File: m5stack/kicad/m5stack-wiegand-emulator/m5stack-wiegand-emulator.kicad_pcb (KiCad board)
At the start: 2 copper layers, 50 x 50 mm, 58 parts, among them J1 2x15 socket header, J2 2x15 pin header, J3 1x5 female, M1 M5 Stack 3.1mm mounting hole, M12 M5 Stack 1.1mm reference hole, M2 M5 Stack 3.1mm mounting hole, M3 M5 Stack 3.1mm mounting hole, M4 M5 Stack 3.1mm mounting hole, M5 M5 Stack 2mm mounting hole, M6 M5 Stack 2mm mounting hole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

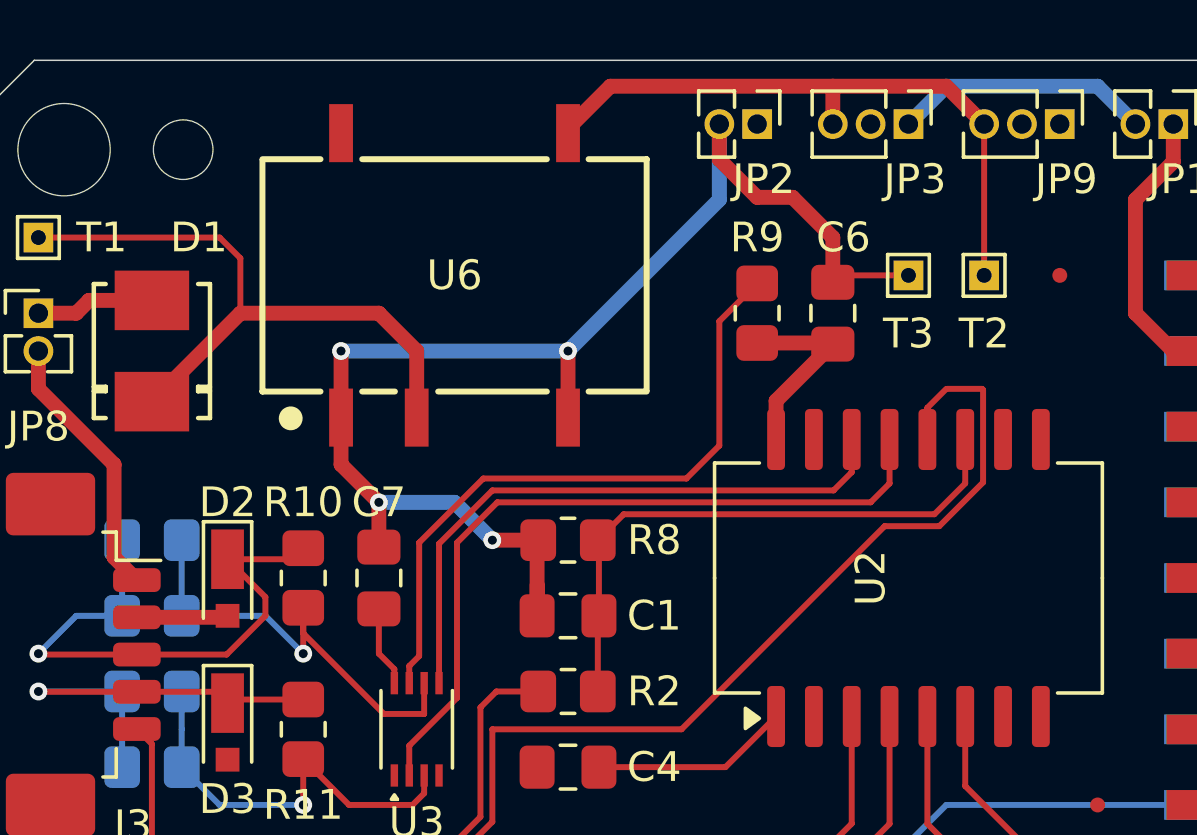
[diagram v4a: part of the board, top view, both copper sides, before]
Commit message: M5: recalculated LED input resistance
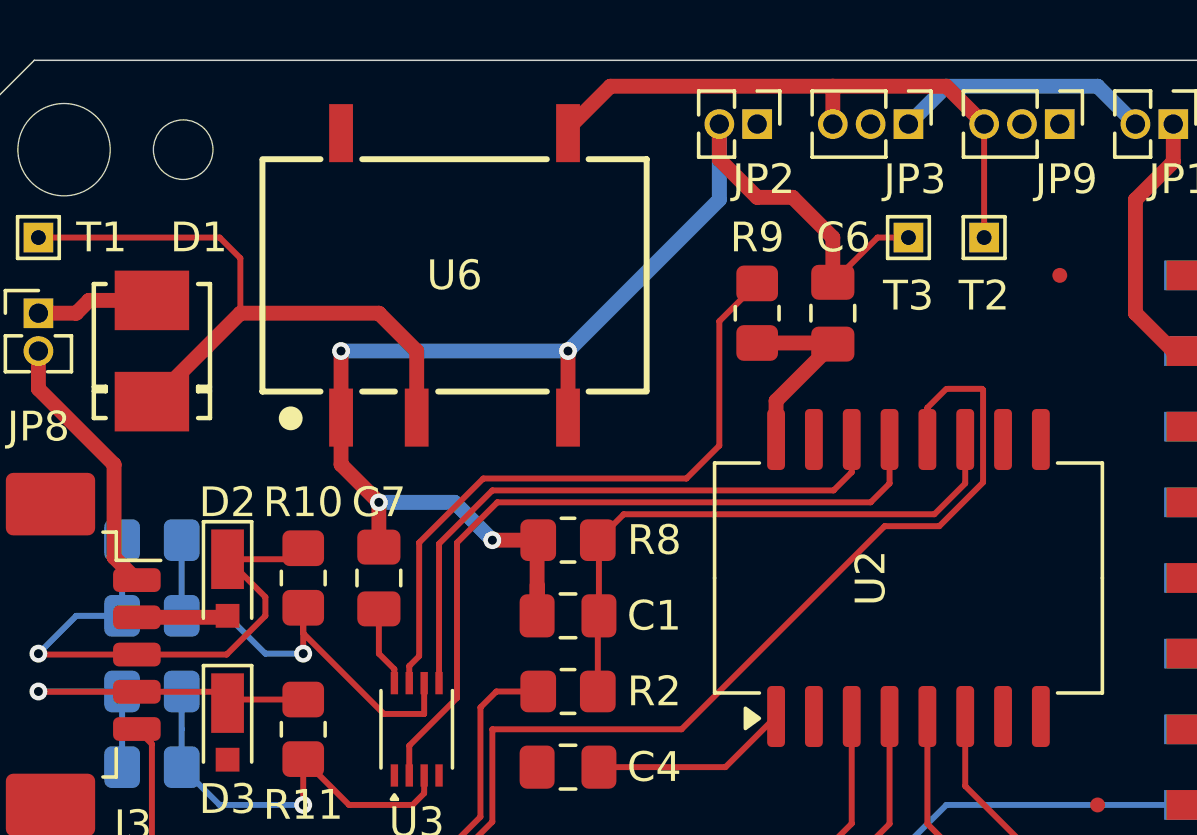
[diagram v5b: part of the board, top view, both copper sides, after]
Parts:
- R13: value 10 -> 1k
- R2: value 470 -> 1k
- moved T2 1.27 mm to (123.2, 69.8)
- moved T3 1.27 mm to (120.7, 69.8)
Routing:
- net +VDC: track 21.6 -> 20.3 mm
- net GND1: track 53.4 -> 53.9 mm
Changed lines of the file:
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@@
     (pad "2" smd rect (at 1.02 0 270) (size 0.8 0.8) (layers "F.Cu" "F.Paste" "F.Mask")
       (net 62 "GND1") (pinfunction "A2") (pintype "passive"))
-    (model "${KICAD6_3DMODEL_DIR}/Diode_SMD.3dshapes/D_MicroSMP_AK.wrl"
+    (model "${KICAD_UHPPOTED}/uhppoted.pretty/MSP5.0A-M3_89A.step" hide
       (offset (xyz 0 0 0))
       (scale (xyz 1 1 1))
-      (rotate (xyz 0 0 0))
+      (rotate (xyz -90 0 0))
+    )
+    (model "${KICAD_UHPPOTED}/uhppoted.pretty/DO-219AD.step"
+      (offset (xyz 0 0 0))
+      (scale (xyz 1 1 1))
+      (rotate (xyz -90 0 0))
     )
   )
@@
     (pad "2" smd rect (at 1.02 0 270) (size 0.8 0.8) (layers "F.Cu" "F.Paste" "F.Mask")
       (net 62 "GND1") (pinfunction "A2") (pintype "passive"))
-    (model "${KICAD6_3DMODEL_DIR}/Diode_SMD.3dshapes/D_MicroSMP_AK.wrl"
+    (model "${KICAD_UHPPOTED}/uhppoted.pretty/MSP5.0A-M3_89A.step" hide
       (offset (xyz 0 0 0))
       (scale (xyz 1 1 1))
-      (rotate (xyz 0 0 0))
+      (rotate (xyz -90 0 0))
+    )
+    (model "${KICAD_UHPPOTED}/uhppoted.pretty/DO-219AD.step"
+      (offset (xyz 0 0 0))
+      (scale (xyz 1 1 1))
+      (rotate (xyz -90 0 0))
     )
   )
@@
     (property "ki_keywords" "diode TVS thyrector")
     (attr smd)
-    (fp_text reference "D2" (at -2.79 0 180) (layer "F.SilkS")
+    (fp_text reference "D2" (at -2.79 0) (layer "F.SilkS")
         (effects (font (size 1 1) (thickness 0.15)))
     )
@@
     (pad "2" smd rect (at 1.02 0 270) (size 0.8 0.8) (layers "F.Cu" "F.Paste" "F.Mask")
       (net 62 "GND1") (pinfunction "A2") (pintype "passive"))
-    (model "${KICAD6_3DMODEL_DIR}/Diode_SMD.3dshapes/D_MicroSMP_AK.wrl"
+    (model "${KICAD_UHPPOTED}/uhppoted.pretty/MSP5.0A-M3_89A.step" hide
       (offset (xyz 0 0 0))
       (scale (xyz 1 1 1))
-      (rotate (xyz 0 0 0))
+      (rotate (xyz -90 0 0))
+    )
+    (model "${KICAD_UHPPOTED}/uhppoted.pretty/DO-219AD.step"
+      (offset (xyz 0 0 0))
+      (scale (xyz 1 1 1))
+      (rotate (xyz -90 0 0))
     )
   )
@@
         (effects (font (size 1 1) (thickness 0.15)) (justify right))
     )
-    (fp_text value "470" (at 0 1.65) (layer "F.Fab") hide
+    (fp_text value "1k" (at 0 1.65) (layer "F.Fab") hide
         (effects (font (size 1 1) (thickness 0.15)))
     )
@@
         (effects (font (size 1 1) (thickness 0.15)))
     )
-    (fp_text value "10" (at 0 1.65 90) (layer "F.Fab") hide
+    (fp_text value "1k" (at 0 1.65 90) (layer "F.Fab") hide
         (effects (font (size 1 1) (thickness 0.15)))
     )
@@
   )
   (footprint "TestPoint:TestPoint_THTPad_1.0x1.0mm_Drill0.5mm" (layer "F.Cu")
-    (at 123.19 71.12 180)
+    (at 123.19 69.85 180)
     (descr "THT rectangular pad as test Point, square 1.0mm side length, hole diameter 0.5mm")
     (tags "test point THT pad rectangle square")
@@
   )
   (footprint "TestPoint:TestPoint_THTPad_1.0x1.0mm_Drill0.5mm" (layer "F.Cu")
-    (at 120.65 71.12 180)
+    (at 120.65 69.85 180)
     (descr "THT rectangular pad as test Point, square 1.0mm side length, hole diameter 0.5mm")
     (tags "test point THT pad rectangle square")
@@
   (segment (start 100.33 83.135256) (end 103.039058 85.844314) (width 0.2) (layer "F.Cu") (net 42))
   (via (at 100.33 83.82) (size 0.6) (drill 0.3) (layers "F.Cu" "B.Cu") (net 42))
+  (segment (start 100.33 83.82) (end 99.06 83.82) (width 0.2) (layer "B.Cu") (net 42))
+  (segment (start 97.79 82.55) (end 96.25 82.55) (width 0.2) (layer "B.Cu") (net 42))
+  (segment (start 99.06 83.82) (end 97.79 82.55) (width 0.2) (layer "B.Cu") (net 42))
   (segment (start 96.25 80.01) (end 96.25 82.55) (width 0.2) (layer "B.Cu") (net 42))
-  (segment (start 99.06 82.55) (end 96.25 82.55) (width 0.2) (layer "B.Cu") (net 42))
-  (segment (start 100.33 83.82) (end 99.06 82.55) (width 0.2) (layer "B.Cu") (net 42))
-  (segment (start 123.19 71.12) (end 123.19 66.04) (width 0.2) (layer "F.Cu") (net 44))
   (segment (start 121.92 64.77) (end 118.11 64.77) (width 0.5) (layer "F.Cu") (net 44))
   (segment (start 123.19 66.04) (end 121.92 64.77) (width 0.5) (layer "F.Cu") (net 44))
+  (segment (start 123.19 69.85) (end 123.19 66.04) (width 0.2) (layer "F.Cu") (net 44))
   (segment (start 110.6425 64.77) (end 109.22 66.1925) (width 0.5) (layer "F.Cu") (net 44))
   (segment (start 109.22 66.1925) (end 109.22 66.345) (width 0.5) (layer "F.Cu") (net 44))
@@
   (segment (start 94.7455 82.6) (end 97.74 82.6) (width 0.5) (layer "F.Cu") (net 62))
   (segment (start 115.57 68.5) (end 114.3 67.23) (width 0.5) (layer "F.Cu") (net 62))
-  (segment (start 120.65 71.12) (end 118.3425 71.12) (width 0.2) (layer "F.Cu") (net 62))
-  (segment (start 118.3425 71.12) (end 118.11 71.3525) (width 0.2) (layer "F.Cu") (net 62))
+  (segment (start 120.65 69.85) (end 119.6125 69.85) (width 0.2) (layer "F.Cu") (net 62))
+  (segment (start 119.6125 69.85) (end 118.11 71.3525) (width 0.2) (layer "F.Cu") (net 62))
   (segment (start 118.11 71.3525) (end 118.11 69.85) (width 0.5) (layer "F.Cu") (net 62))
   (segment (start 102.87 78.74) (end 101.6 77.47) (width 0.5) (layer "F.Cu") (net 62))

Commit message: M5: routing PWR
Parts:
- moved JP2 10.2 mm to (125.7, 66.0)
- moved JP9 8.89 mm to (116.8, 66.0)
- moved R1 2.68 mm to (108.0, 101.6), turned to -90 degrees
- moved T2 1.27 mm to (123.2, 71.1)
- moved T3 1.27 mm to (120.7, 71.1)
- moved C6 1.27 mm to (116.8, 72.4)
- moved JP3 1.27 mm to (121.9, 66.0)
- moved R9 1.27 mm to (114.3, 72.4)
- moved JP5 0.65 mm to (119.4, 102.9)
- moved JP4 0.62 mm to (119.4, 105.4)
- moved JP6 0.62 mm to (119.4, 100.3)
- moved JP7 0.62 mm to (119.4, 97.8)
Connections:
- R1 pad 10: Net-(JP4-B) -> Net-(JP7-B)
- R1 pad 2: GND -> Net-(JP6-B)
- R1 pad 3: Net-(R1B-R2.2) -> Net-(JP5-B)
- R1 pad 4: Net-(R1C-R3.2) -> Net-(JP4-B)
- R1 pad 5: Net-(R1D-R4.2) -> GND
- R1 pad 7: Net-(JP7-B) -> Net-(R1E-R5.2)
- R1 pad 8: Net-(JP6-B) -> Net-(R1F-R6.2)
- R1 pad 9: Net-(JP5-B) -> Net-(R1G-R7.2)
- U1 pad 15: Net-(R1B-R2.2) -> Net-(R1E-R5.2)
- U1 pad 16: Net-(R1C-R3.2) -> Net-(R1F-R6.2)
- U1 pad 17: Net-(R1D-R4.2) -> Net-(R1G-R7.2)
- U2 pad 3: Net-(R1D-R4.2) -> Net-(R1G-R7.2)
- U2 pad 4: Net-(R1C-R3.2) -> Net-(R1F-R6.2)
- U2 pad 5: Net-(R1B-R2.2) -> Net-(R1E-R5.2)
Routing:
- net +5V: track 2.54 -> 98.6 mm
- net +3V3: track 6.65 -> 41.9 mm
- net VISO: track 6.60 -> 39.4 mm
- net Net-(R1B-R2.2): track 26.8 -> 0.00 mm
- net Net-(R1E-R5.2): track 0.00 -> 26.8 mm
- net Net-(R1F-R6.2): track 0.00 -> 25.1 mm
- net Net-(R1C-R3.2): track 24.5 -> 0.00 mm
- net GND: track 15.9 -> 39.9 mm, vias 3 -> 5
- net Net-(JP9-C): track 2.71 -> 26.1 mm
- net Net-(JP4-B): track 10.2 -> 33.2 mm
- net Net-(R1G-R7.2): track 0.00 -> 22.9 mm
- net Net-(R1D-R4.2): track 21.6 -> 0.00 mm
- net GND1: track 53.9 -> 36.0 mm, vias 4 -> 10
- net Net-(JP5-B): track 9.39 -> 26.8 mm
- net Net-(JP6-B): track 6.82 -> 22.3 mm
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- added copper zone on B.Cu, net GND1

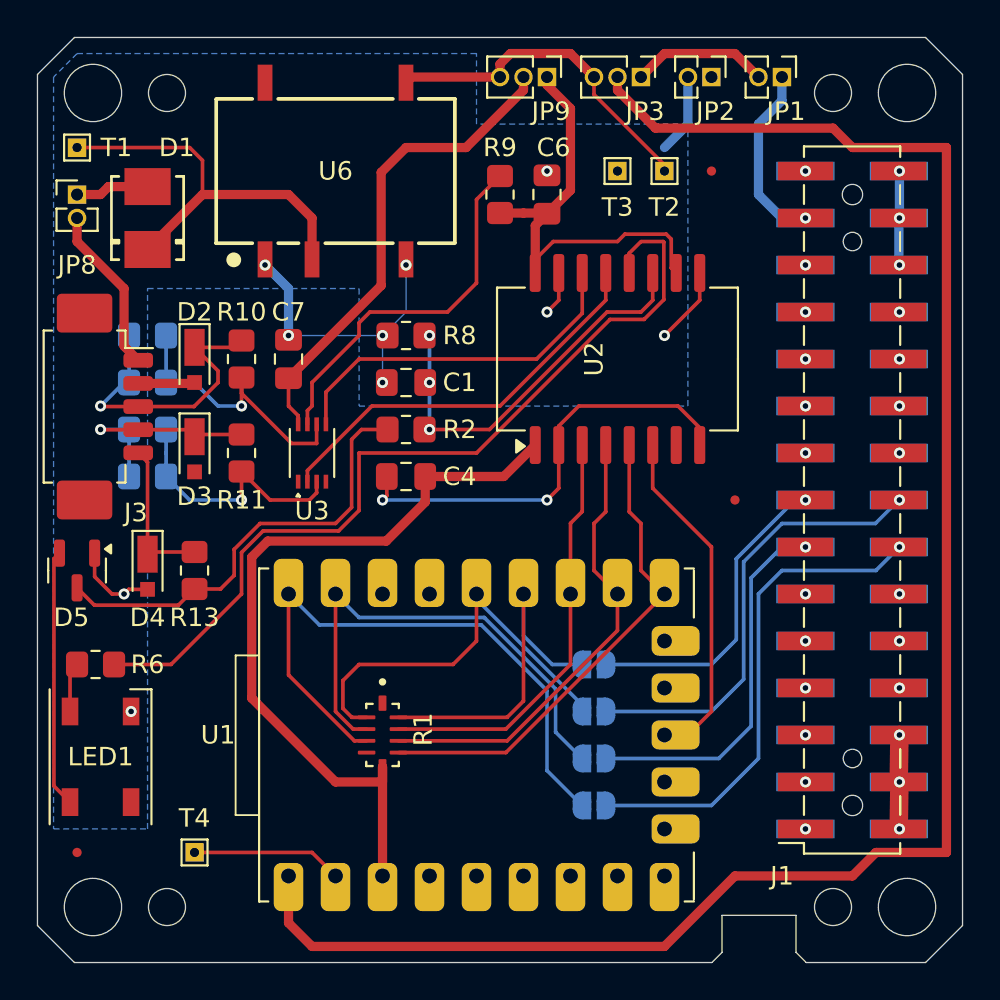
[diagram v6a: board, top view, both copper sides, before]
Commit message: M5: PCB routed and DRC'd
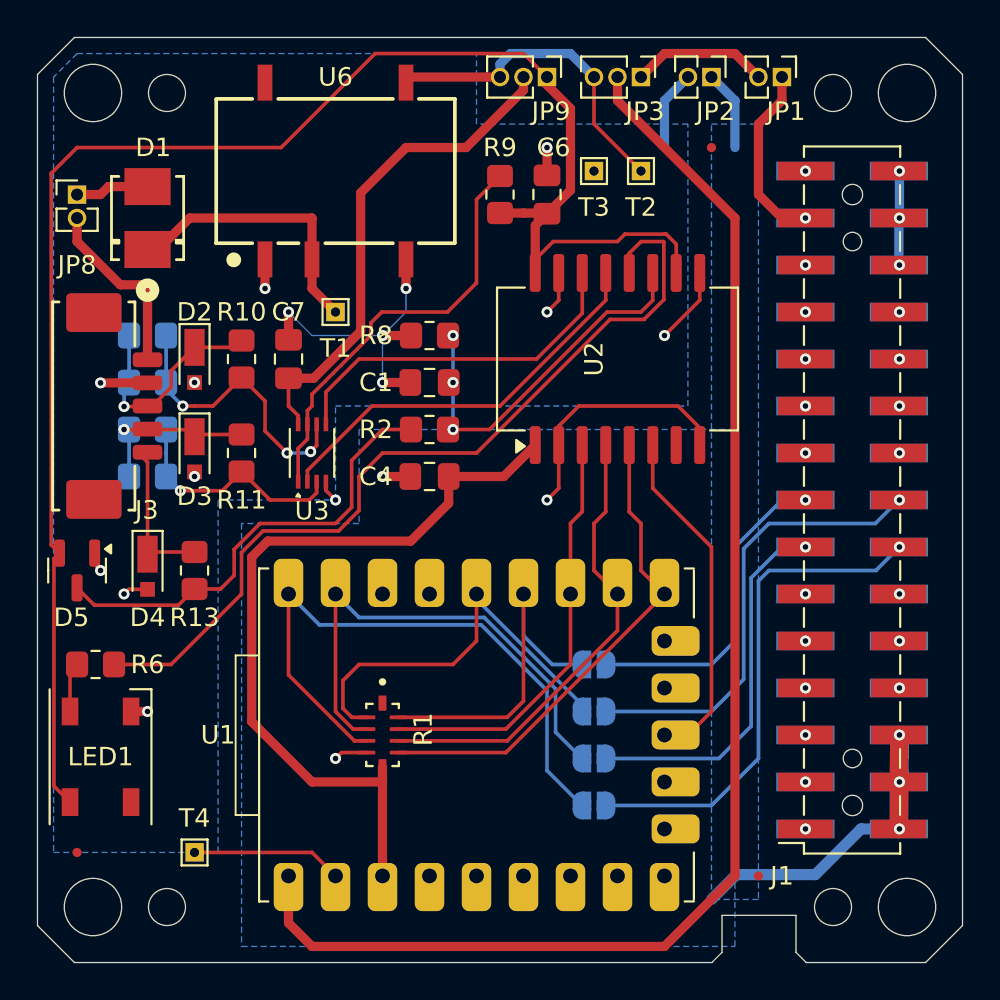
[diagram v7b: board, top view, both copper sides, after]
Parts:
- J3: footprint Connector_Molex:Molex_PicoBlade_53261-0571_1x05-1MP_P1.25mm_Horizontal -> uhppoted:Molex 532610571
- moved F1 20.4 mm to (128.3, 109.2)
- moved T1 16.6 mm to (105.4, 78.7)
- moved G*** 10.9 mm to (106.7, 68.6), turned to 0 degrees
- moved F2 1.27 mm to (125.7, 69.8)
- moved T3 1.27 mm to (119.4, 71.1)
- moved C1 1.27 mm to (110.5, 82.5)
- moved C4 1.27 mm to (110.5, 87.6)
- moved R2 1.27 mm to (110.5, 85.1)
- moved R8 1.27 mm to (110.5, 80.0)
- moved T2 1.27 mm to (121.9, 71.1)
- turned J3 to 90 degrees
- renumbered REF** to M10, REF** to M11
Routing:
- net VISO: track 39.4 -> 90.1 mm
- net +5V: track 98.6 -> 74.6 mm
- net GND: track 39.9 -> 54.1 mm, vias 5 -> 6
- net Net-(D1-K): track 21.8 -> 15.2 mm
- net /DI: track 16.6 -> 12.3 mm
- net Net-(U3-1OE): track 20.2 -> 23.1 mm
- net GND1: track 36.0 -> 38.7 mm, vias 10 -> 15
- net Net-(U2-IND): track 22.9 -> 20.2 mm
- net /DO: track 12.2 -> 9.64 mm
- net Net-(U3-2Y): track 14.1 -> 12.8 mm
- net /12VDC: track 9.06 -> 9.86 mm
- net Net-(JP9-C): track 26.1 -> 26.9 mm
- net Net-(U2-OUTC): track 47.3 -> 46.6 mm
- net Net-(D5-COM): track 24.1 -> 24.7 mm
- net +VDC: track 18.4 -> 17.9 mm
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- added copper zone on B.Cu, net GND

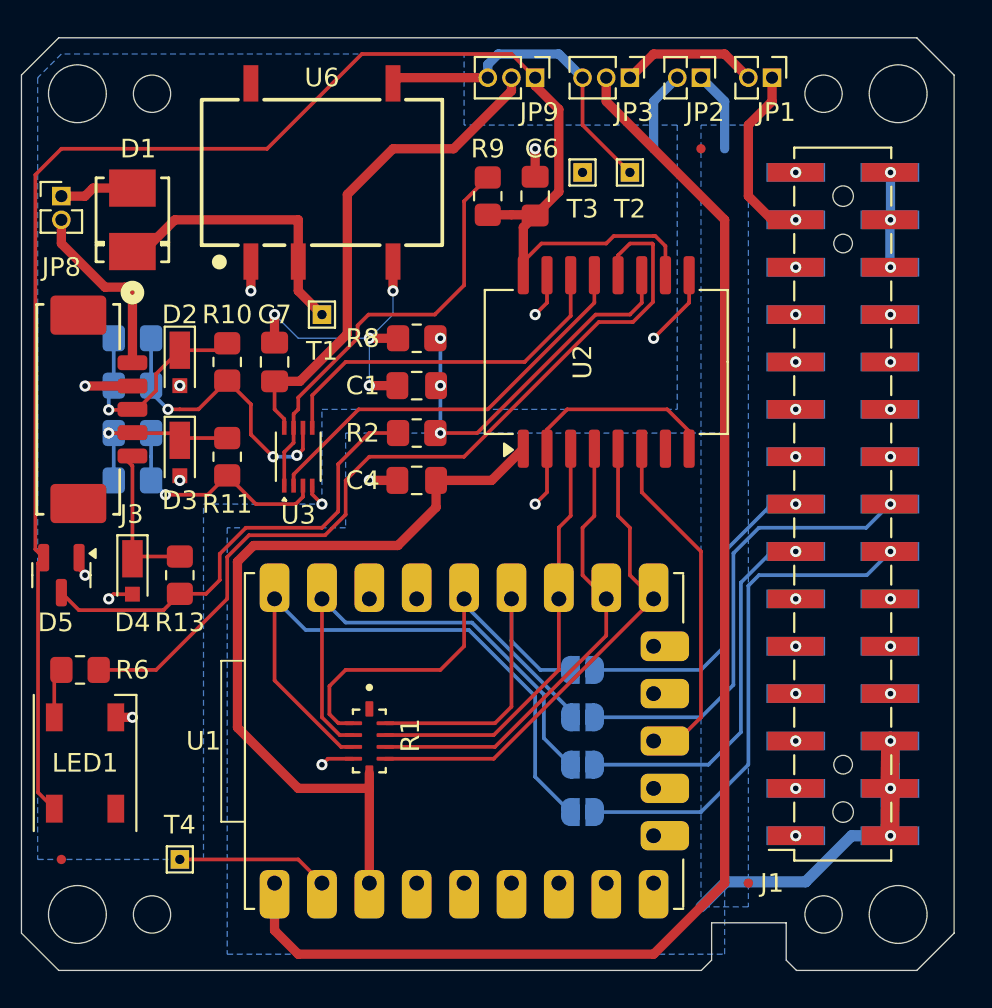
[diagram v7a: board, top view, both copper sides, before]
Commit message: M5: replaced J1+J2 with single THT connector
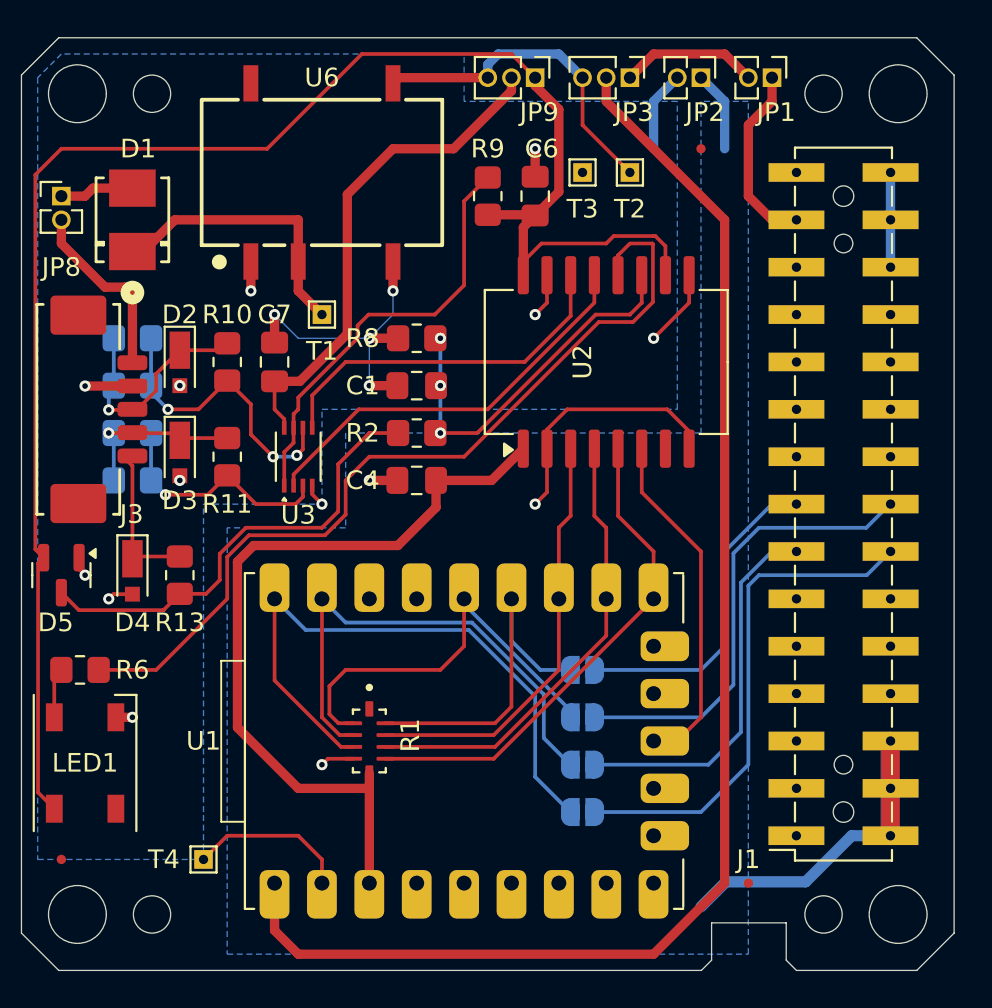
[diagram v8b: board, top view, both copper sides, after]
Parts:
- removed J2: 2x15 pin header, Connector_PinHeader_2.54mm:PinHeader_2x15_P2.54mm_Vertical_SMD
- removed M10, M11: M5 Stack 1mm reference hole, uhppoted:M5 Stack 1mm reference hole
- removed M12, M9: M5 Stack 1.1mm reference hole, uhppoted:M5 Stack 1.1mm reference hole
- J1: footprint Connector_PinSocket_2.54mm:PinSocket_2x15_P2.54mm_Vertical_SMD -> uhppoted:M5 Bus connector
- moved T4 1.27 mm to (99.1, 108.0)
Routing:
- net GND: track 54.1 -> 51.9 mm, vias 6 -> 3
- net /TXD1: track 20.9 -> 20.2 mm, vias 1 -> 0
- net /RXD1: track 27.9 -> 27.3 mm, vias 1 -> 0
- net /TXD2: track 18.1 -> 17.4 mm, vias 1 -> 0
- net /RXD2: track 25.8 -> 25.2 mm, vias 1 -> 0
- net Net-(R1F-R6.2): track 25.1 -> 24.6 mm
- net /HPWR: track 5.09 -> 5.05 mm, vias 3 -> 0
- net /SDA: vias 1 -> 0
- net /SCLK: vias 1 -> 0
- net /SCL: vias 1 -> 0
- net /RESET: vias 1 -> 0
- net /MOSI: vias 1 -> 0
- net /MISO: vias 1 -> 0
- net /IO9: vias 1 -> 0
- net /IO8: vias 1 -> 0
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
